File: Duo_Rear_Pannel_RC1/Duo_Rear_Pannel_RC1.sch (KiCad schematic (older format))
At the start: 49 parts, among them CN1 CONN_PANNEL_2X2, CN2 CONN_PANNEL_2X2, J1 USB_A, J2 RJ45_CHAIN, J3 USB_B, J4 MIDI_CONN, J5 MIDI_CONN, J6 JACK_3P_2.5MM, P1 HEADER_8X2, P2 KK3.96_2PIN, Q1 BS870, Q2 BS870, U1 RT9728BH, U2 6N137

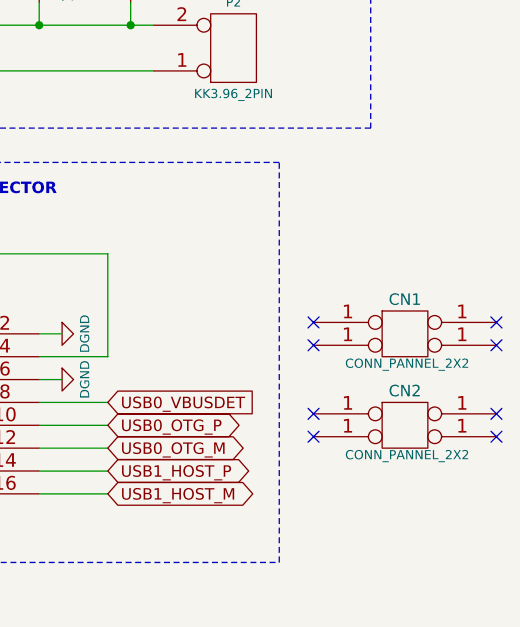
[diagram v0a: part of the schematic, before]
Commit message: Implementing RCA1 schematic  modifications for new layout. Backup commit.
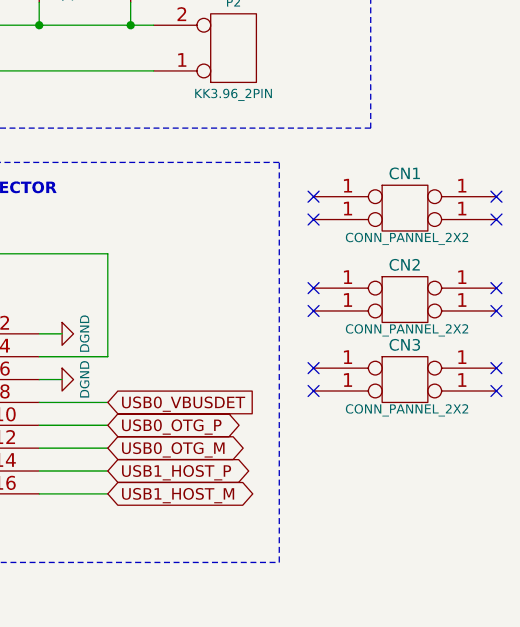
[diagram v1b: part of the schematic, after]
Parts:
- added CN3: CONN_PANNEL_2X2, CONN_PANNEL, symbol CONN_PANNEL_2X2
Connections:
- no-connect marks 14 -> 18
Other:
- moved on the sheet: CN1, CN2
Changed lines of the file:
@@
 LIBS:Duo_Rear_Pannel_RC1
 LIBS:Duo_Rear_Pannel_RC1-cache
-EELAYER 27 0
+EELAYER 24 0
 EELAYER END
 $Descr A4 11693 8268
@@
 L CONN_PANNEL_2X2 CN1
 U 1 1 53433D6E
-P 10700 6050
-F 0 "CN1" H 10700 6200 50  0000 C CNN
-F 1 "CONN_PANNEL_2X2" H 10710 5920 40  0000 C CNN
-F 2 "CONN_PANNEL" H 10700 6050 60  0001 C CNN
-F 3 "" H 10700 6050 60  0000 C CNN
-	1    10700 6050
+P 10700 5500
+F 0 "CN1" H 10700 5650 50  0000 C CNN
+F 1 "CONN_PANNEL_2X2" H 10710 5370 40  0000 C CNN
+F 2 "CONN_PANNEL" H 10700 5500 60  0001 C CNN
+F 3 "" H 10700 5500 60  0000 C CNN
+	1    10700 5500
 	1    0    0    -1
 $EndComp
@@
 L CONN_PANNEL_2X2 CN2
 U 1 1 5343416D
-P 10700 6450
-F 0 "CN2" H 10700 6600 50  0000 C CNN
-F 1 "CONN_PANNEL_2X2" H 10710 6320 40  0000 C CNN
-F 2 "CONN_PANNEL" H 10700 6450 60  0001 C CNN
-F 3 "" H 10700 6450 60  0000 C CNN
-	1    10700 6450
-	1    0    0    -1
-$EndComp
-NoConn ~ 10300 6000
-NoConn ~ 10300 6100
-NoConn ~ 10300 6400
-NoConn ~ 10300 6500
-NoConn ~ 11100 6500
-NoConn ~ 11100 6400
-NoConn ~ 11100 6100
-NoConn ~ 11100 6000
+P 10700 5900
+F 0 "CN2" H 10700 6050 50  0000 C CNN
+F 1 "CONN_PANNEL_2X2" H 10710 5770 40  0000 C CNN
+F 2 "CONN_PANNEL" H 10700 5900 60  0001 C CNN
+F 3 "" H 10700 5900 60  0000 C CNN
+	1    10700 5900
+	1    0    0    -1
+$EndComp
+NoConn ~ 10300 5450
+NoConn ~ 10300 5550
+NoConn ~ 10300 5850
+NoConn ~ 10300 5950
+NoConn ~ 11100 5950
+NoConn ~ 11100 5850
+NoConn ~ 11100 5550
+NoConn ~ 11100 5450
 $Comp
 L C C11
@@
 Wire Wire Line
 	8800 6950 8700 6950
+$Comp
+L CONN_PANNEL_2X2 CN3
+U 1 1 537A7C16
+P 10700 6250
+F 0 "CN3" H 10700 6400 50  0000 C CNN
+F 1 "CONN_PANNEL_2X2" H 10710 6120 40  0000 C CNN
+F 2 "CONN_PANNEL" H 10700 6250 60  0001 C CNN
+F 3 "" H 10700 6250 60  0000 C CNN
+	1    10700 6250
+	1    0    0    -1
+$EndComp
+NoConn ~ 10300 6200
+NoConn ~ 10300 6300
+NoConn ~ 11100 6300
+NoConn ~ 11100 6200
 $EndSCHEMATC

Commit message: Finished RCA1 schematic of the Baseboard and the Pannelboard with USB OTG. Board dimensions, most footprint attribution and major placement implemented in layout. Learning GIT!
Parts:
- removed C1, C10, C13, C3, C5, C8, C9: 100nF_X7R, SM0603, symbol C
- removed C11: 100nF_MF, CAP_FILM_12.6X4.5_L10, symbol C
- removed C12, C2, C4, C6, C7: 100uF, CAP_RAD_5MM, symbol CP1
- removed CN1, CN2, CN3: CONN_PANNEL_2X2, CONN_PANNEL, symbol CONN_PANNEL_2X2
- removed D1, D4: PRTR5V0U2X, symbol PRTR5V0U2X
- removed D2, D3: MMSZ5242B, SOD123_, symbol ZENERSMALL
- removed D5: 1N4148, SOD323, symbol DIODE
- removed FB1, FB2, FB3, FB4: FB_150OHM800mA, SM0805, symbol FERRITE_BEAD
- removed GND1: CONN_1, symbol CONN_1
- removed J1: USB_A, USB_A_73725, symbol USB_A
- removed J2: RJ45_CHAIN, RJ45_TFN2_88_1, symbol RJ45_CHAIN
- removed J3: USB_B, symbol USB_B
- removed J4, J5: MIDI_CONN, CON_MIDI_SDS-50J, symbol MIDI_CONN
- removed J6: JACK_3P_2.5MM, PJ-002B, symbol JACK_3P
- removed L1, L2: CM_NOISE_FILTER, symbol CM_NOISE_FILTER
- removed P1: HEADER_8X2, pin_array_8x2, symbol CONN_8X2
- removed P2: KK3.96_2PIN, KK3.96_2PIN, symbol CONN_2
- removed Q1, Q2: BS870, SOT23, symbol MOS_N_SOT23
- removed R1: 120R, SM0805, symbol R
- removed R10, R3, R4, R9: 1k, SM0603, symbol R
- removed R2: 226k_1%, SM0603, symbol R
- removed R5: 10k, SM0603, symbol R
- removed R6, R7, R8: 220R, SM0805, symbol R
- removed U1: RT9728BH, symbol RT9728A
- removed U2: 6N137, SMD_8, symbol 6N137
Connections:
- net labels removed: +5V, +9V, DGND, MIDI_IN_UART, MIDI_OUT_UART, RS422_A, RS422_B, USB0_OTG_M, USB0_OTG_P, USB0_VBUSDET, USB1_DRV, USB1_HOST_M, USB1_HOST_P, USB1_PWR_FAULT
- wire segments 168 -> 0
- no-connect marks 18 -> 0
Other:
- note removed: "BASEBOARD CONNECTOR"
- note removed: "CONTROL CHAIN"
- note removed: "MIDI IN"
- note removed: "MIDI OUT"
- note removed: "POWER IN"
- note removed: "USB HOST"
- note removed: "USB OTG DEVICE ONLY"
